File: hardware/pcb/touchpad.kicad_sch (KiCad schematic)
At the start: 1 part, among them U7 DRV2605LDGS

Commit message: started cleaning up schematic
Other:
- company: (none) -> Gensis
- title: (none) -> Touchpad
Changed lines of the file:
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@@
 	(generator_version "10.0")
 	(paper "A4")
+	(title_block
+		(title "Touchpad")
+		(rev "v1.0.0")
+		(company "Gensis")
+	)
 	(bus_entry
 		(at 109.22 93.98)

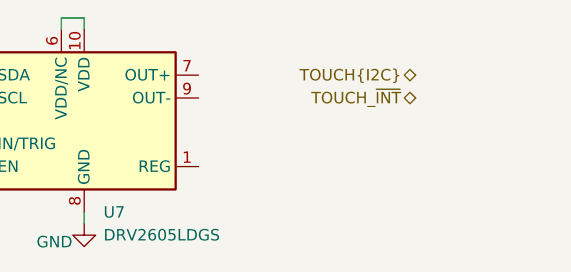
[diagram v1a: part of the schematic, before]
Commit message: main board: fixed schematic errors, made sama7 symbol better
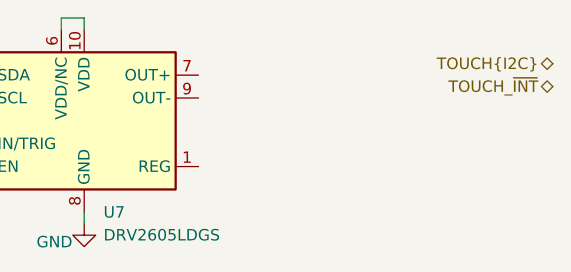
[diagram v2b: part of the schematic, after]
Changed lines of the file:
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@@
 	(hierarchical_label "TOUCH_~{INT}"
 		(shape bidirectional)
-		(at 167.64 96.52 180)
+		(at 182.88 95.25 180)
 		(effects
 			(font
@@
 	(hierarchical_label "TOUCH{I2C}"
 		(shape bidirectional)
-		(at 167.64 93.98 180)
+		(at 182.88 92.71 180)
 		(effects
 			(font

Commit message: mainboard: adde notes
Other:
- note added: "Connector for the trackpad depends on the layout of the PCB Will be chosen later"
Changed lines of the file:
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@@
 		(company "Gensis")
+	)
+	(text "Connector for the trackpad depends on the layout of the PCB\n\nWill be chosen later"
+		(exclude_from_sim no)
+		(at 201.93 92.71 0)
+		(effects
+			(font
+				(size 1.27 1.27)
+			)
+			(justify left)
+		)
 	)
 	(bus_entry
@@
 	(hierarchical_label "TOUCH_~{INT}"
 		(shape bidirectional)
-		(at 182.88 95.25 180)
+		(at 199.39 93.98 180)
 		(effects
 			(font
@@
 	(hierarchical_label "TOUCH{I2C}"
 		(shape bidirectional)
-		(at 182.88 92.71 180)
+		(at 199.39 91.44 180)
 		(effects
 			(font

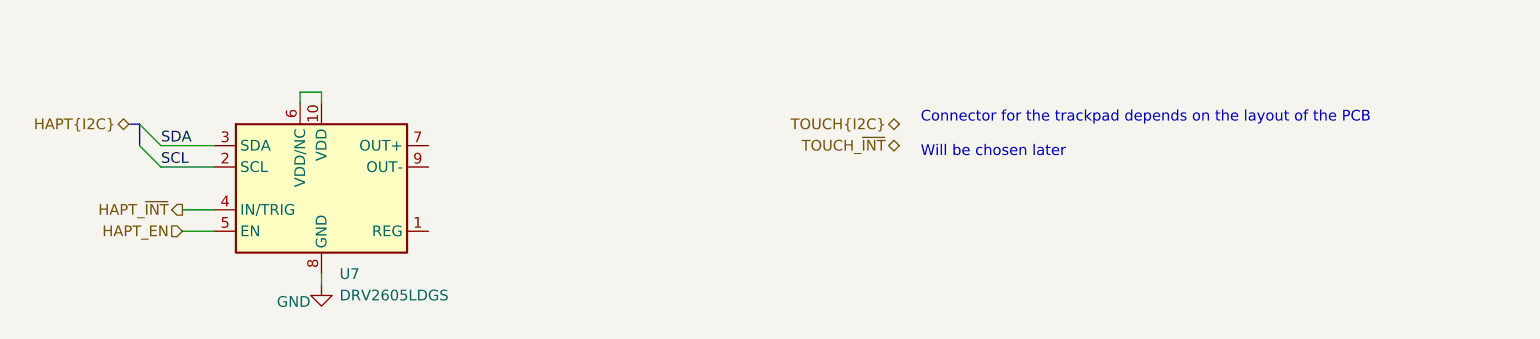
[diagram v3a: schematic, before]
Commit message: mainboard: finished touchpad schematic
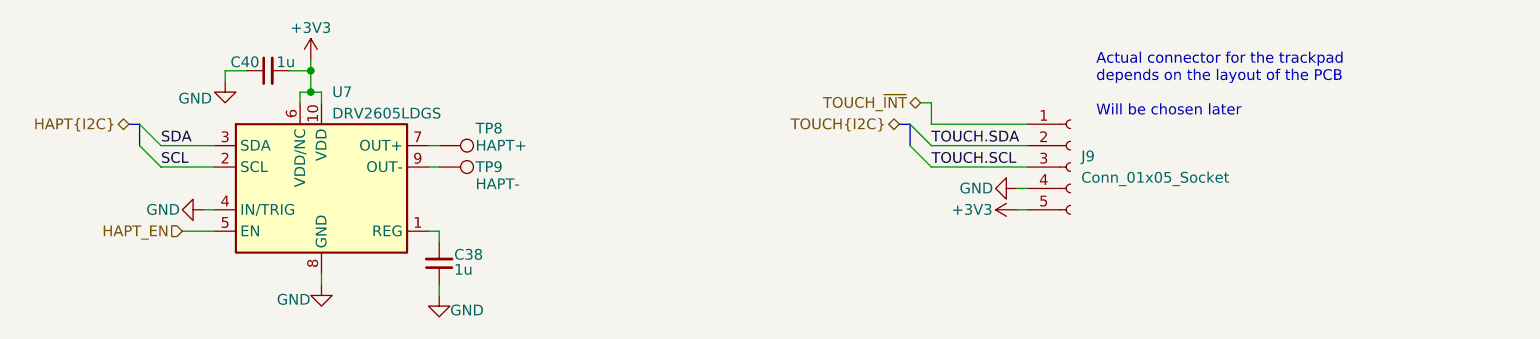
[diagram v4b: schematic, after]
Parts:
- added C38, C40: 1u, Capacitor_SMD:C_0402_1005Metric, symbol Device:C_Small
- added J9: Conn_01x05_Socket, Package_DIP:DIP-20_W7.62mm, symbol Connector:Conn_01x05_Socket
- added TP8: HAPT+, symbol Connector:TestPoint
- added TP9: HAPT-, symbol Connector:TestPoint
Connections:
- net HAPT_~{INT} is gone; now on net GND: U7.4 (IN/TRIG)
- net GND: now also C38.1, C40.1, J9.4 (Pin_4)
- net TOUCH_~{INT}: now also J9.1 (Pin_1)
- net at U7.1 (REG): now also C38.2
- net +3V3: now reaches U7.10 (VDD), U7.6 (VDD/NC)
- net +3V3: now also C40.2, J9.5 (Pin_5)
- net at U7.7 (OUT+): now also TP8.1
- net at U7.9 (OUT-): now also TP9.1
- new net TOUCH.SCL: J9.3 (Pin_3)
- new net TOUCH.SDA: J9.2 (Pin_2)
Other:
- note added: "Actual connector for the trackpad depends on the layout of the PCB Will be chosen later"
- note removed: "Connector for the trackpad depends on the layout of the PCB Will be chosen later"

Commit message: mainboard: reannotated schematic
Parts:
- renumbered C40 to C121, C38 to C122
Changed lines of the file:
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@@
 		(in_pos_files yes)
 		(dnp no)
-		(property "Reference" "#PWR097"
+		(property "Reference" "#PWR0135"
 			(at 130.81 116.84 0)
 			(hide yes)
@@
 			(project "meko"
 				(path "/da54f10a-146b-4941-a9c7-55c7173bb101/7a0a8608-fb91-40ee-9ae1-ac8166908c37"
-					(reference "#PWR097")
+					(reference "#PWR0135")
 					(unit 1)
 				)
@@
 		(in_pos_files yes)
 		(dnp no)
-		(property "Reference" "#PWR0135"
+		(property "Reference" "#PWR0132"
 			(at 207.01 99.06 0)
 			(hide yes)
@@
 			(project "meko"
 				(path "/da54f10a-146b-4941-a9c7-55c7173bb101/7a0a8608-fb91-40ee-9ae1-ac8166908c37"
-					(reference "#PWR0135")
+					(reference "#PWR0132")
 					(unit 1)
 				)
@@
 		(in_pos_files yes)
 		(dnp no)
-		(property "Reference" "C40"
+		(property "Reference" "C121"
 			(at 123.444 84.074 90)
 			(show_name no)
@@
 			(project "meko"
 				(path "/da54f10a-146b-4941-a9c7-55c7173bb101/7a0a8608-fb91-40ee-9ae1-ac8166908c37"
-					(reference "C40")
+					(reference "C121")
 					(unit 1)
 				)
@@
 		(in_pos_files yes)
 		(dnp no)
-		(property "Reference" "C38"
+		(property "Reference" "C122"
 			(at 146.558 106.934 0)
 			(show_name no)
@@
 			(project "meko"
 				(path "/da54f10a-146b-4941-a9c7-55c7173bb101/7a0a8608-fb91-40ee-9ae1-ac8166908c37"
-					(reference "C38")
+					(reference "C122")
 					(unit 1)
 				)
@@
 		(in_pos_files yes)
 		(dnp no)
-		(property "Reference" "#PWR0132"
+		(property "Reference" "#PWR0136"
 			(at 144.78 118.11 0)
 			(hide yes)
@@
 			(project "meko"
 				(path "/da54f10a-146b-4941-a9c7-55c7173bb101/7a0a8608-fb91-40ee-9ae1-ac8166908c37"
-					(reference "#PWR0132")
+					(reference "#PWR0136")
 					(unit 1)
 				)
@@
 		(in_pos_files yes)
 		(dnp no)
-		(property "Reference" "#PWR0137"
+		(property "Reference" "#PWR0131"
 			(at 119.38 92.71 0)
 			(hide yes)
@@
 			(project "meko"
 				(path "/da54f10a-146b-4941-a9c7-55c7173bb101/7a0a8608-fb91-40ee-9ae1-ac8166908c37"
-					(reference "#PWR0137")
+					(reference "#PWR0131")
 					(unit 1)
 				)
@@
 		(in_pos_files yes)
 		(dnp no)
-		(property "Reference" "#PWR0136"
+		(property "Reference" "#PWR0130"
 			(at 129.54 87.63 0)
 			(hide yes)
@@
 			(project "meko"
 				(path "/da54f10a-146b-4941-a9c7-55c7173bb101/7a0a8608-fb91-40ee-9ae1-ac8166908c37"
-					(reference "#PWR0136")
-					(unit 1)
-				)
+					(reference "#PWR0130")
+					(unit 1)
+				)

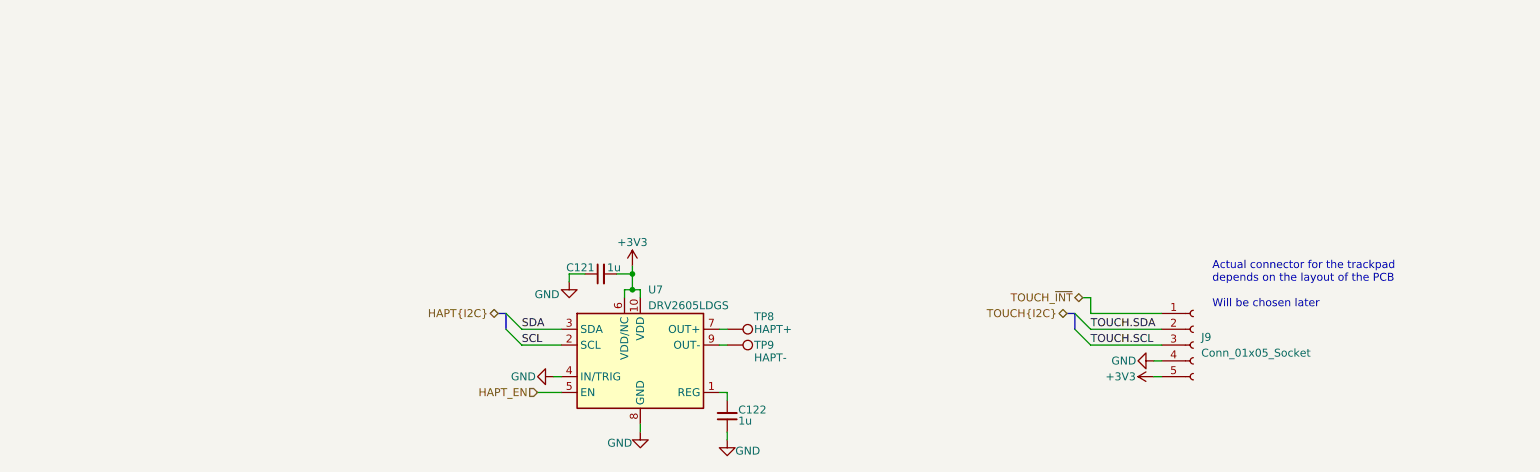
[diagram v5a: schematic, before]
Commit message: mainboard: added sections to touchpad schematic
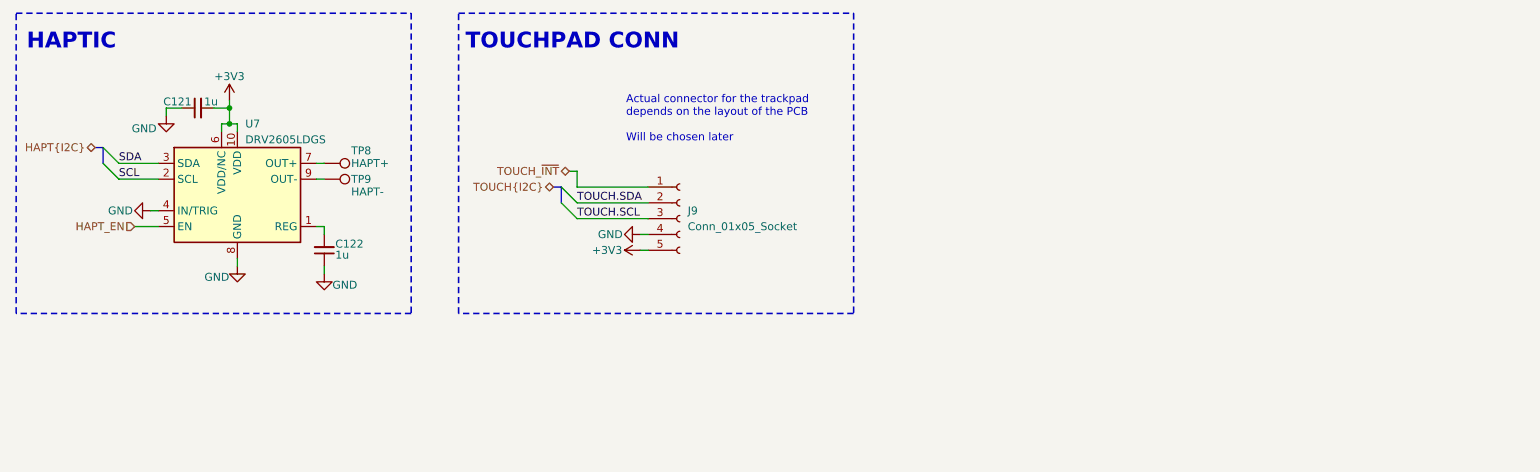
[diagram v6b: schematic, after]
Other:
- note added: "HAPTIC"
- note added: "TOUCHPAD CONN"
- moved on the sheet: C121, C122, J9, TP8, TP9, U7

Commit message: mainboard: removed wrong footprint from touchpad conn
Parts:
- J9: footprint Package_DIP:DIP-20_W7.62mm -> (none)
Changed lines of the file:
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@@
 			)
 		)
-		(property "Footprint" "Package_DIP:DIP-20_W7.62mm"
+		(property "Footprint" ""
 			(at 137.16 76.2 0)
 			(hide yes)

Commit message: assigned missing footprints
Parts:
- TP8, TP9: footprint (none) -> TestPoint:TestPoint_Pad_D1.0mm
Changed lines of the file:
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@@
 			)
 		)
-		(property "Footprint" ""
+		(property "Footprint" "TestPoint:TestPoint_Pad_D1.0mm"
 			(at 80.01 74.93 0)
 			(hide yes)
@@
 			)
 		)
-		(property "Footprint" ""
+		(property "Footprint" "TestPoint:TestPoint_Pad_D1.0mm"
 			(at 80.01 72.39 0)
 			(hide yes)
